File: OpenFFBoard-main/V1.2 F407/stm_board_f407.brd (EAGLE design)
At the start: 60 x 60 mm, 60 parts, among them J1 10118193-0001LF, SW1 TL3342F160QG/TR, SW2 TL3342F160QG/TR, U1 STM32F407VGT6, U2 TJA1051T/3, U3 LM1117, X1 8MHz

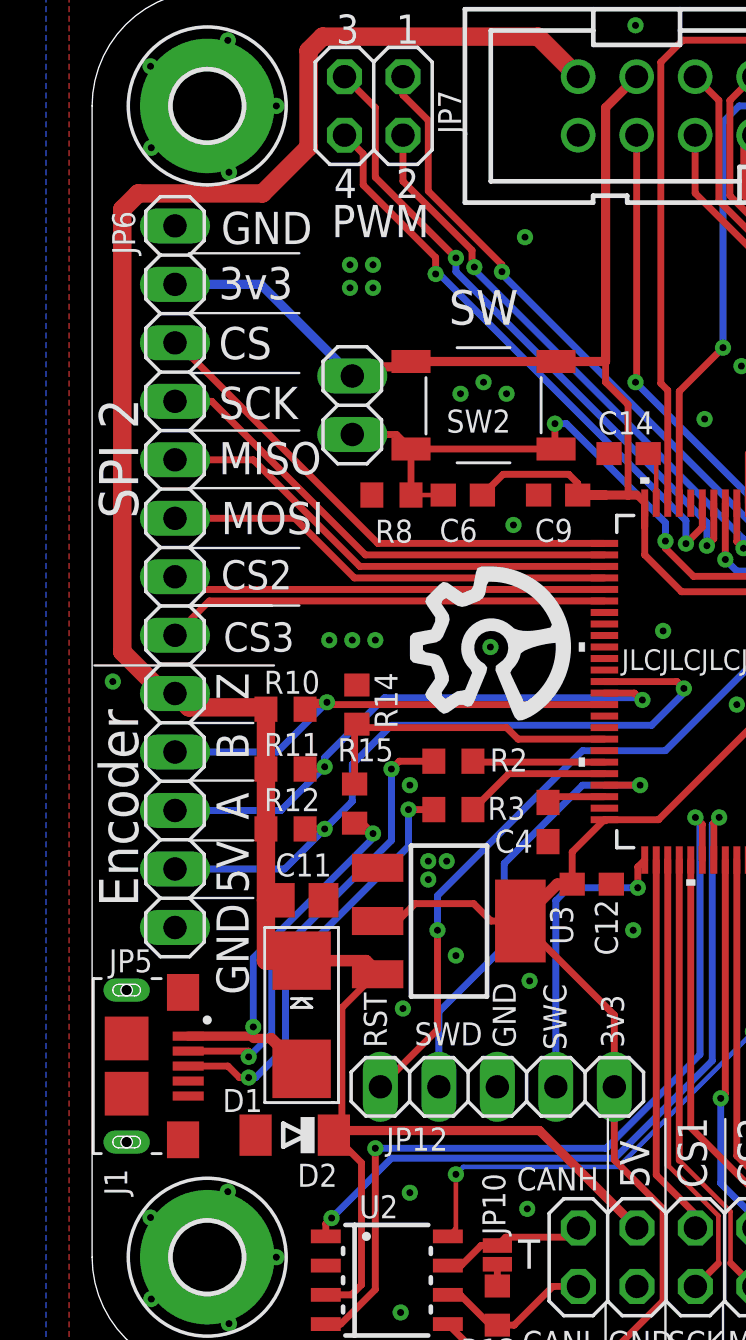
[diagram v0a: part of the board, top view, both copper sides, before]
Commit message: Updated crystal capacitor value
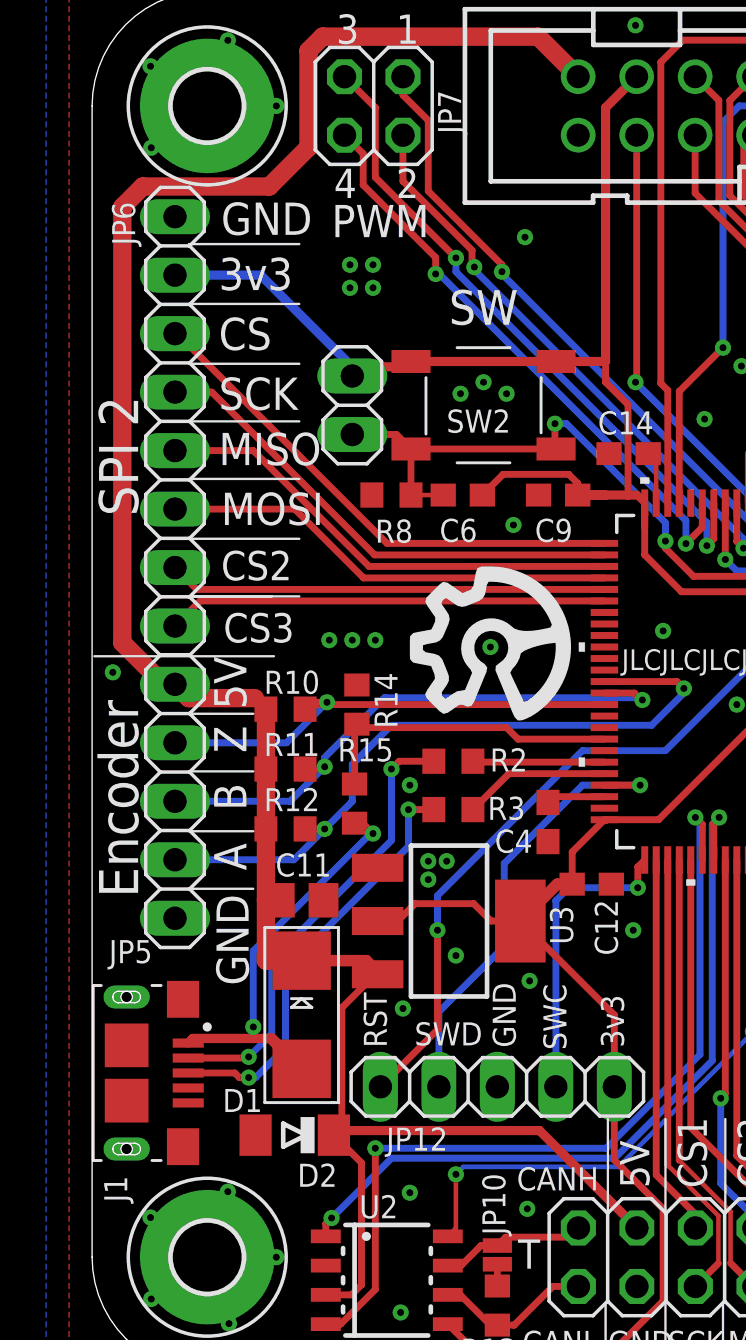
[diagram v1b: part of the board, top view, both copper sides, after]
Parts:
- C1, C2: value 30pF -> 15pF
- moved JP6 0.40 mm to (3.60, -18.7)
- moved JP5 0.40 mm to (3.60, -35.2)
- moved J1 0.30 mm to (1.50, -47.0)

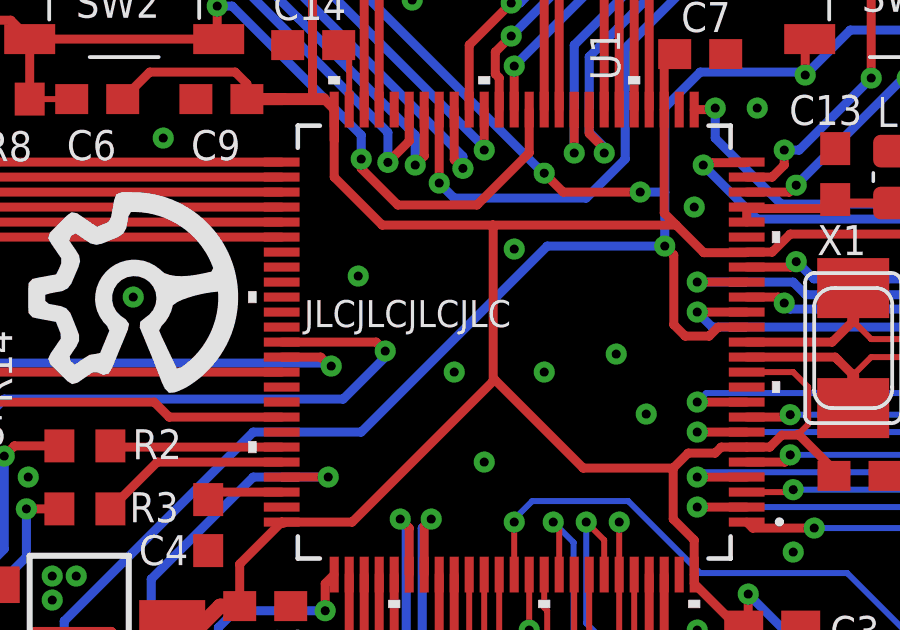
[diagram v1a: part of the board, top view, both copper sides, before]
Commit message: Fixed tmc silkscreen (Resistor names, labels)
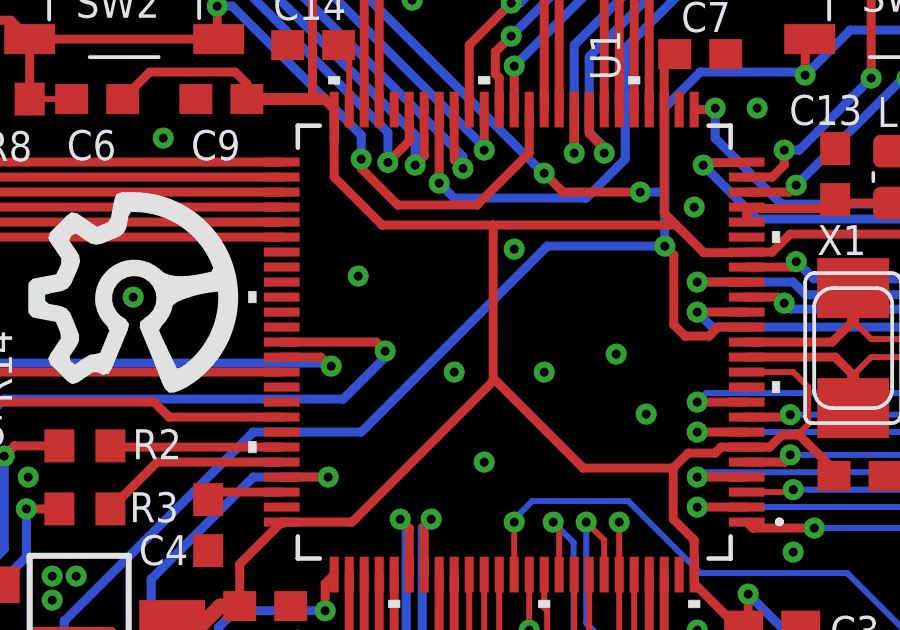
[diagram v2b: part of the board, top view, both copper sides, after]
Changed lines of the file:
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@@
 <drawing>
 <settings>
-<setting alwaysvectorfont="no"/>
+<setting alwaysvectorfont="yes"/>
 <setting verticaltext="up"/>
 </settings>
@@
 <layer number="27" name="tValues" color="7" fill="1" visible="no" active="yes"/>
 <layer number="28" name="bValues" color="7" fill="1" visible="no" active="yes"/>
-<layer number="29" name="tStop" color="7" fill="3" visible="no" active="yes"/>
-<layer number="30" name="bStop" color="7" fill="6" visible="no" active="yes"/>
-<layer number="31" name="tCream" color="7" fill="4" visible="yes" active="yes"/>
-<layer number="32" name="bCream" color="7" fill="5" visible="yes" active="yes"/>
+<layer number="29" name="tStop" color="7" fill="3" visible="yes" active="yes"/>
+<layer number="30" name="bStop" color="7" fill="6" visible="yes" active="yes"/>
+<layer number="31" name="tCream" color="7" fill="4" visible="no" active="yes"/>
+<layer number="32" name="bCream" color="7" fill="5" visible="no" active="yes"/>
 <layer number="33" name="tFinish" color="6" fill="3" visible="no" active="yes"/>
 <layer number="34" name="bFinish" color="6" fill="6" visible="no" active="yes"/>
@@
 <text x="53.6" y="-46.1" size="1.4" layer="21" rot="R90">CLIP</text>
 <text x="45.6" y="-46.1" size="1.4" layer="21" rot="R90">PWR</text>
-<text x="23" y="-29.5" size="0.9" layer="21">JLCJLCJLCJLC</text>
+<text x="35" y="-29.5" size="0.9" layer="22" rot="MR0">JLCJLCJLCJLC</text>
 <wire x1="24.9" y1="-57" x2="24.9" y2="-60" width="0.1016" layer="21"/>
 <wire x1="22.3" y1="-57" x2="22.3" y2="-60" width="0.1016" layer="21"/>
@@
 <param name="mlMinCreamFrame" value="0mil"/>
 <param name="mlMaxCreamFrame" value="0mil"/>
-<param name="mlViaStopLimit" value="0mil"/>
+<param name="mlViaStopLimit" value="0.4mm"/>
 <param name="srRoundness" value="0"/>
 <param name="srMinRoundness" value="0mil"/>
